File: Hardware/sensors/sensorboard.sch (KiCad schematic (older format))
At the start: 0 parts

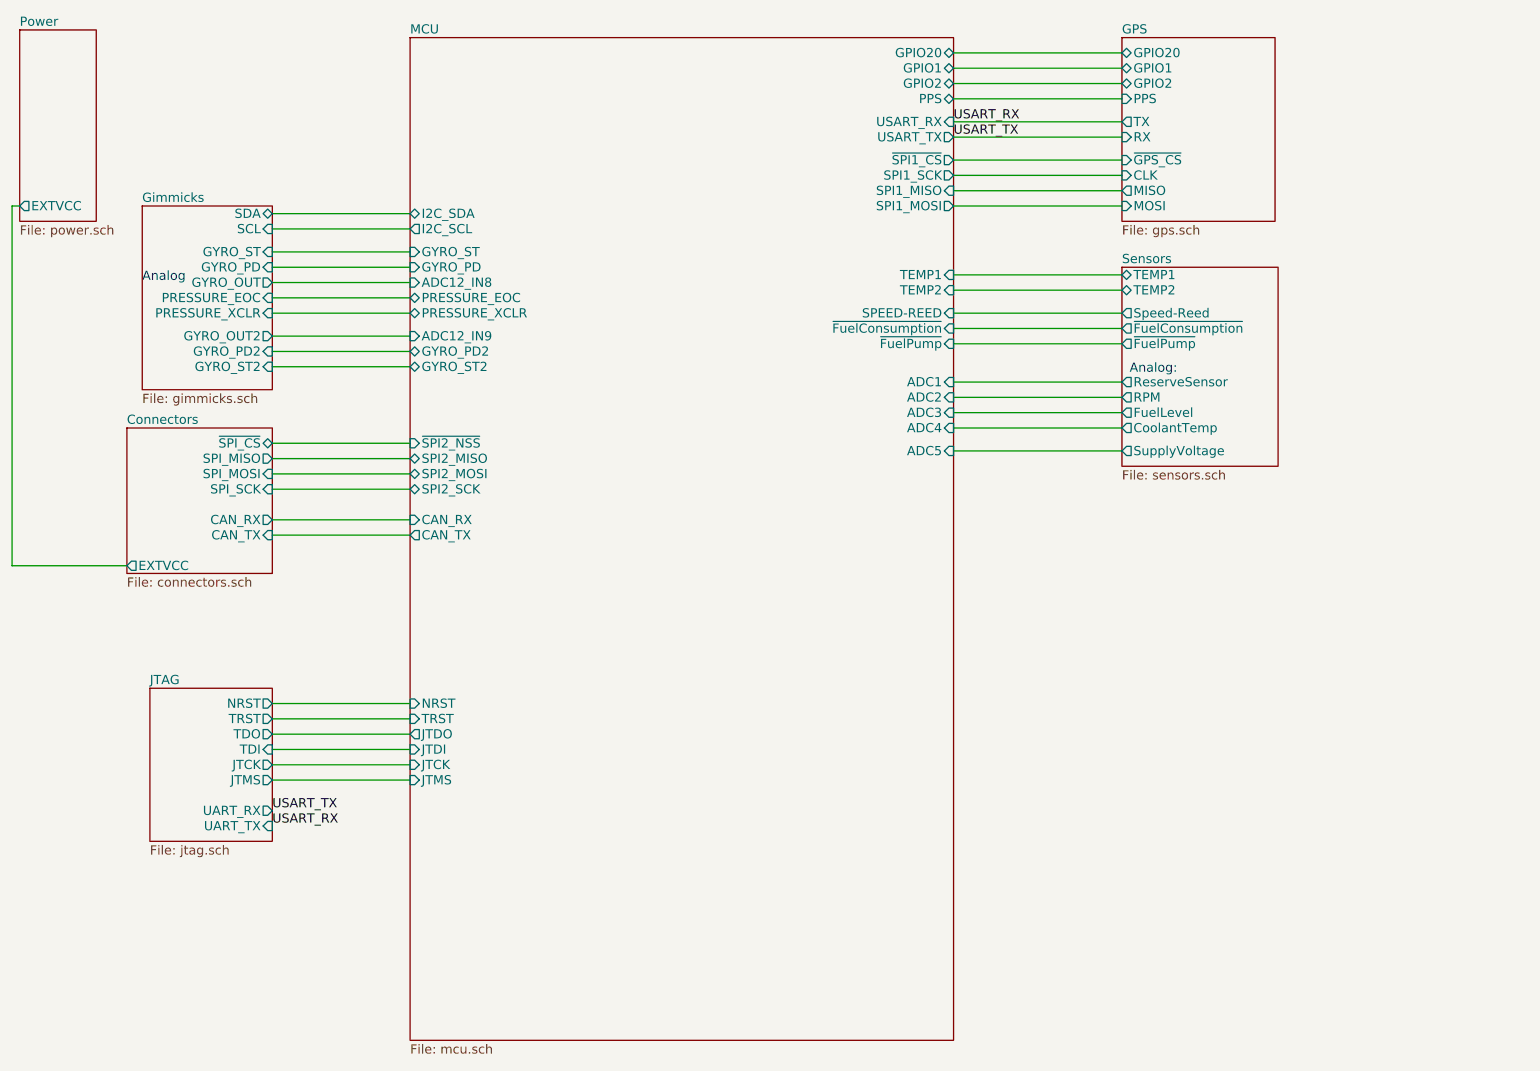
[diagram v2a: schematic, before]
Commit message: mounting holes and test version of the bottom of the housing for the sensors pcb
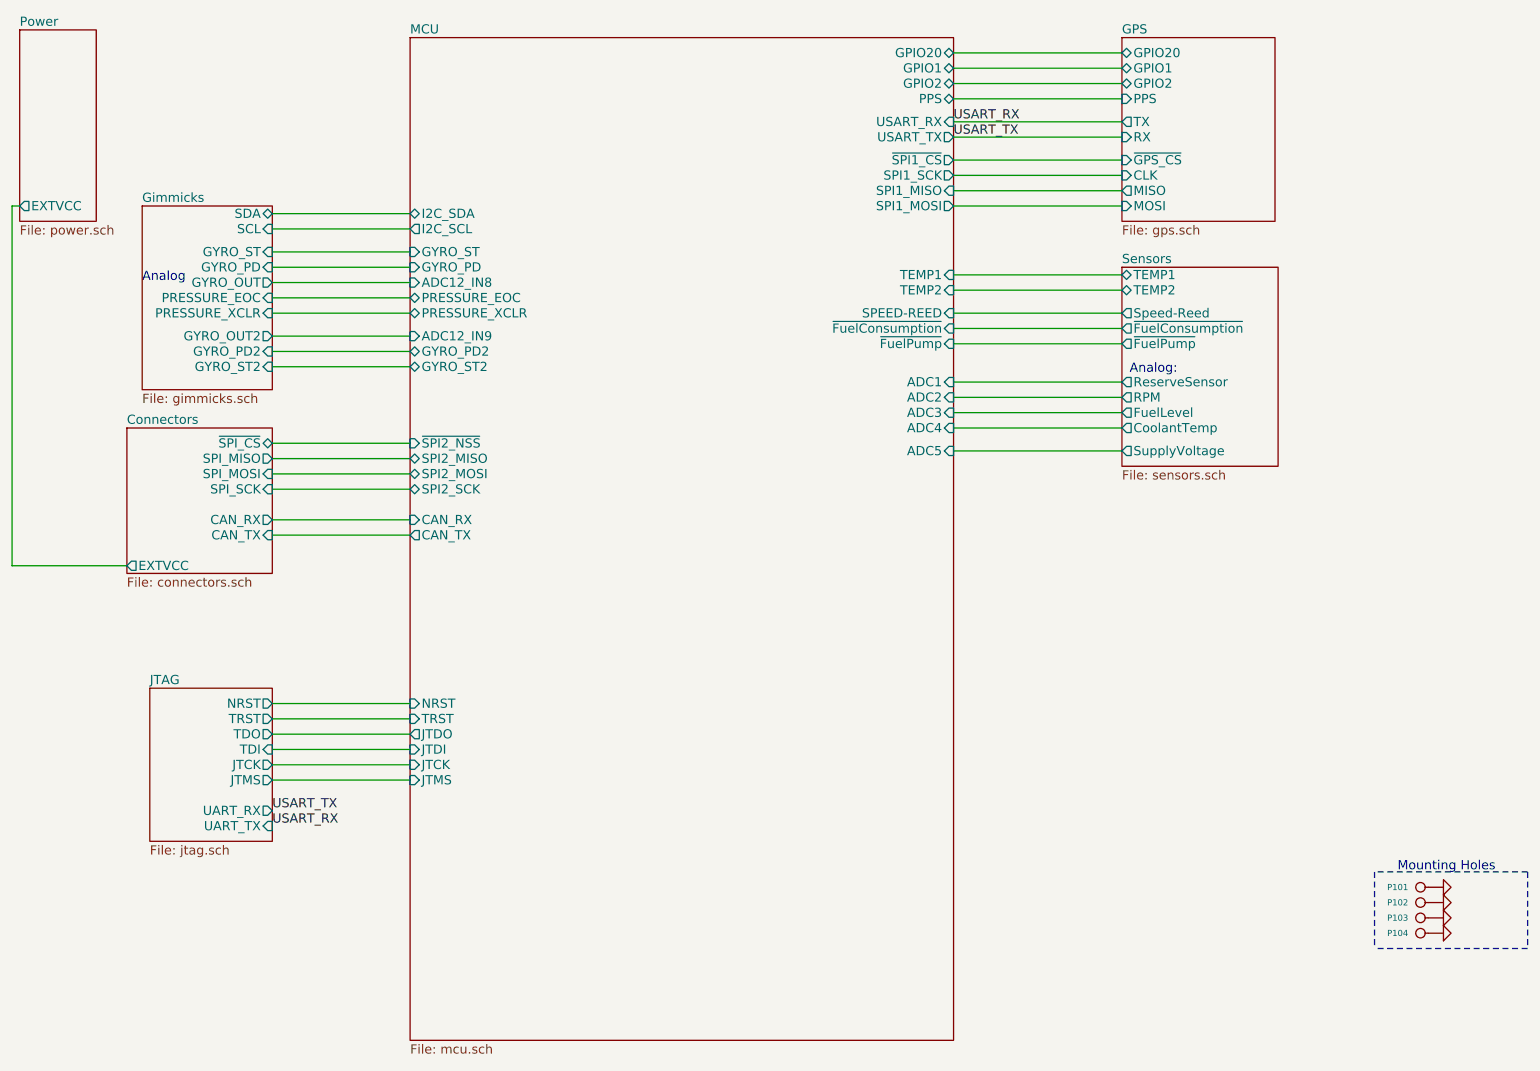
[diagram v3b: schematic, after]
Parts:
- added P101, P102, P103, P104: Mount, symbol CONN_1
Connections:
- new net GND: P101.1, P102.1, P103.1, P104.1
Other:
- note added: "Mounting Holes"
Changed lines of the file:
@@
-EESchema Schematic File Version 2  date Do 17 Mär 2011 20:34:15 CET
+EESchema Schematic File Version 2  date So 20 Mär 2011 20:56:18 CET
 LIBS:power
 LIBS:device
@@
 Sheet 1 8
 Title ""
-Date "17 mar 2011"
+Date "20 mar 2011"
 Rev ""
 Comp ""
@@
 Comment4 ""
 $EndDescr
+Wire Notes Line
+	10450 6650 9450 6650
+Wire Notes Line
+	10450 6150 10450 6650
+Wire Notes Line
+	10450 6150 9450 6150
+Wire Wire Line
+	2250 2850 3150 2850
+Wire Wire Line
+	2250 2750 3150 2750
+Wire Wire Line
+	2250 2650 3150 2650
+Wire Wire Line
+	2250 1950 3150 1950
+Wire Wire Line
+	2250 1850 3150 1850
+Wire Wire Line
+	6700 1100 7800 1100
+Wire Wire Line
+	6700 1000 7800 1000
+Wire Wire Line
+	6700 900  7800 900
+Wire Wire Line
+	6700 800  7800 800
+Wire Wire Line
+	6700 1350 7800 1350
+Wire Wire Line
+	6700 1250 7800 1250
+Wire Wire Line
+	1300 4150 550  4150
+Wire Wire Line
+	550  4150 550  1800
+Wire Wire Line
+	550  1800 600  1800
+Wire Wire Line
+	2250 3950 3150 3950
+Wire Wire Line
+	2250 3850 3150 3850
+Wire Wire Line
+	6700 2950 7800 2950
+Wire Wire Line
+	6700 3050 7800 3050
+Wire Wire Line
+	6700 3150 7800 3150
+Wire Wire Line
+	6700 3250 7800 3250
+Wire Wire Line
+	2250 3350 3150 3350
+Wire Wire Line
+	2250 3450 3150 3450
+Wire Wire Line
+	2250 3550 3150 3550
+Wire Wire Line
+	2250 3650 3150 3650
+Wire Wire Line
+	2250 5050 3150 5050
+Wire Wire Line
+	2250 5150 3150 5150
+Wire Wire Line
+	2250 5250 3150 5250
+Wire Wire Line
+	2250 5350 3150 5350
+Wire Wire Line
+	2250 5450 3150 5450
+Wire Wire Line
+	2250 5550 3150 5550
+Wire Wire Line
+	6700 1500 7800 1500
+Wire Wire Line
+	6700 1600 7800 1600
+Wire Wire Line
+	6700 1700 7800 1700
+Wire Wire Line
+	6700 1800 7800 1800
+Wire Wire Line
+	6700 2250 7800 2250
+Wire Wire Line
+	6700 2350 7800 2350
+Wire Wire Line
+	6700 2500 7800 2500
+Wire Wire Line
+	6700 2600 7800 2600
+Wire Wire Line
+	6700 2700 7800 2700
+Wire Wire Line
+	2250 2100 3150 2100
+Wire Wire Line
+	2250 2200 3150 2200
+Wire Wire Line
+	2250 2300 3150 2300
+Wire Wire Line
+	2250 2400 3150 2400
+Wire Wire Line
+	2250 2500 3150 2500
 Wire Wire Line
 	7800 3400 6700 3400
-Wire Wire Line
-	2250 2500 3150 2500
-Wire Wire Line
-	2250 2400 3150 2400
-Wire Wire Line
-	2250 2300 3150 2300
-Wire Wire Line
-	2250 2200 3150 2200
-Wire Wire Line
-	2250 2100 3150 2100
-Wire Wire Line
-	6700 2700 7800 2700
-Wire Wire Line
-	6700 2600 7800 2600
-Wire Wire Line
-	6700 2500 7800 2500
-Wire Wire Line
-	6700 2350 7800 2350
-Wire Wire Line
-	6700 2250 7800 2250
-Wire Wire Line
-	6700 1800 7800 1800
-Wire Wire Line
-	6700 1700 7800 1700
-Wire Wire Line
-	6700 1600 7800 1600
-Wire Wire Line
-	6700 1500 7800 1500
-Wire Wire Line
-	2250 5550 3150 5550
-Wire Wire Line
-	2250 5450 3150 5450
-Wire Wire Line
-	2250 5350 3150 5350
-Wire Wire Line
-	2250 5250 3150 5250
-Wire Wire Line
-	2250 5150 3150 5150
-Wire Wire Line
-	2250 5050 3150 5050
-Wire Wire Line
-	2250 3650 3150 3650
-Wire Wire Line
-	2250 3550 3150 3550
-Wire Wire Line
-	2250 3450 3150 3450
-Wire Wire Line
-	2250 3350 3150 3350
-Wire Wire Line
-	6700 3250 7800 3250
-Wire Wire Line
-	6700 3150 7800 3150
-Wire Wire Line
-	6700 3050 7800 3050
-Wire Wire Line
-	6700 2950 7800 2950
-Wire Wire Line
-	2250 3850 3150 3850
-Wire Wire Line
-	2250 3950 3150 3950
-Wire Wire Line
-	600  1800 550  1800
-Wire Wire Line
-	550  1800 550  4150
-Wire Wire Line
-	550  4150 1300 4150
-Wire Wire Line
-	6700 1250 7800 1250
-Wire Wire Line
-	6700 1350 7800 1350
-Wire Wire Line
-	6700 800  7800 800
-Wire Wire Line
-	6700 900  7800 900
-Wire Wire Line
-	6700 1000 7800 1000
-Wire Wire Line
-	6700 1100 7800 1100
-Wire Wire Line
-	2250 1850 3150 1850
-Wire Wire Line
-	2250 1950 3150 1950
-Wire Wire Line
-	2250 2650 3150 2650
-Wire Wire Line
-	2250 2750 3150 2750
-Wire Wire Line
-	2250 2850 3150 2850
+Wire Notes Line
+	9450 6150 9450 6650
+$Comp
+L GND #PWR01
+U 1 1 4D865BA3
+P 9900 6550
+F 0 "#PWR01" H 9900 6550 30  0001 C CNN
+F 1 "GND" H 9900 6480 30  0001 C CNN
+	1    9900 6550
+	0    -1   -1   0
+$EndComp
+$Comp
+L GND #PWR02
+U 1 1 4D865B9D
+P 9900 6450
+F 0 "#PWR02" H 9900 6450 30  0001 C CNN
+F 1 "GND" H 9900 6380 30  0001 C CNN
+	1    9900 6450
+	0    -1   -1   0
+$EndComp
+$Comp
+L GND #PWR03
+U 1 1 4D865B9B
+P 9900 6350
+F 0 "#PWR03" H 9900 6350 30  0001 C CNN
+F 1 "GND" H 9900 6280 30  0001 C CNN
+	1    9900 6350
+	0    -1   -1   0
+$EndComp
+$Comp
+L GND #PWR04
+U 1 1 4D865B99
+P 9900 6250
+F 0 "#PWR04" H 9900 6250 30  0001 C CNN
+F 1 "GND" H 9900 6180 30  0001 C CNN
+	1    9900 6250
+	0    -1   -1   0
+$EndComp
+$Comp
+L CONN_1 P104
+U 1 1 4D865B93
+P 9750 6550
+F 0 "P104" H 9830 6550 40  0000 L CNN
+F 1 "Mount" H 9750 6605 30  0001 C CNN
+	1    9750 6550
+	-1   0    0    1
+$EndComp
+$Comp
+L CONN_1 P103
+U 1 1 4D865B91
+P 9750 6450
+F 0 "P103" H 9830 6450 40  0000 L CNN
+F 1 "Mount" H 9750 6505 30  0001 C CNN
+	1    9750 6450
+	-1   0    0    1
+$EndComp
+$Comp
+L CONN_1 P102
+U 1 1 4D865B8F
+P 9750 6350
+F 0 "P102" H 9830 6350 40  0000 L CNN
+F 1 "Mount" H 9750 6405 30  0001 C CNN
+	1    9750 6350
+	-1   0    0    1
+$EndComp
+$Comp
+L CONN_1 P101
+U 1 1 4D865B8C
+P 9750 6250
+F 0 "P101" H 9830 6250 40  0000 L CNN
+F 1 "Mount" H 9750 6305 30  0001 C CNN
+	1    9750 6250
+	-1   0    0    1
+$EndComp
+Text Notes 9600 6150 0    60   ~ 0
+Mounting Holes
 Text Label 2250 5750 0    60   ~ 0
 USART_TX

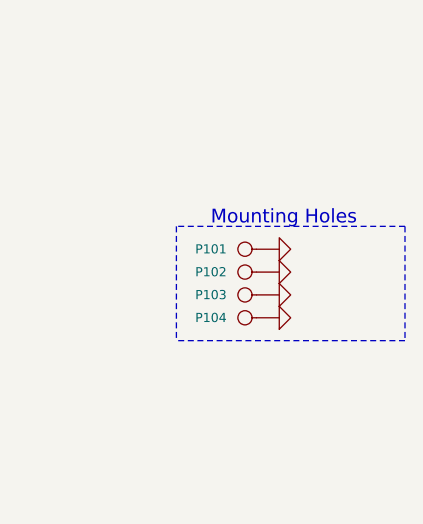
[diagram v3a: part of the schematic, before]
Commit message: using adc instead of analog multiplexer for sensor board, some work on mcu board
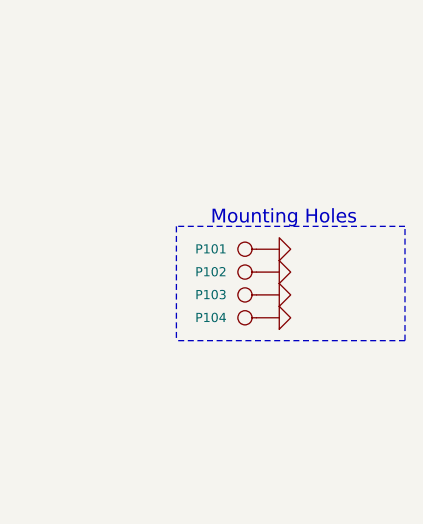
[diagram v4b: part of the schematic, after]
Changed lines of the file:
@@
-EESchema Schematic File Version 2  date So 20 Mär 2011 20:56:18 CET
+EESchema Schematic File Version 2  date Mi 18 Mai 2011 15:58:13 CEST
 LIBS:power
 LIBS:device
@@
 Sheet 1 8
 Title ""
-Date "20 mar 2011"
+Date "18 may 2011"
 Rev ""
 Comp ""
@@
 	10450 6650 9450 6650
 Wire Notes Line
-	10450 6150 10450 6650
+	10450 6650 10450 6150
 Wire Notes Line
 	10450 6150 9450 6150
